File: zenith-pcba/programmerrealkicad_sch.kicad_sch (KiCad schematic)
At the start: 16 parts, among them SW1 G4R152312, U1 XC7A50T-CSG325, U3 CH347T, U4 TPS54302DDCT, U5 TPS54302DDCT, X1 SX5B8.000F1520F30

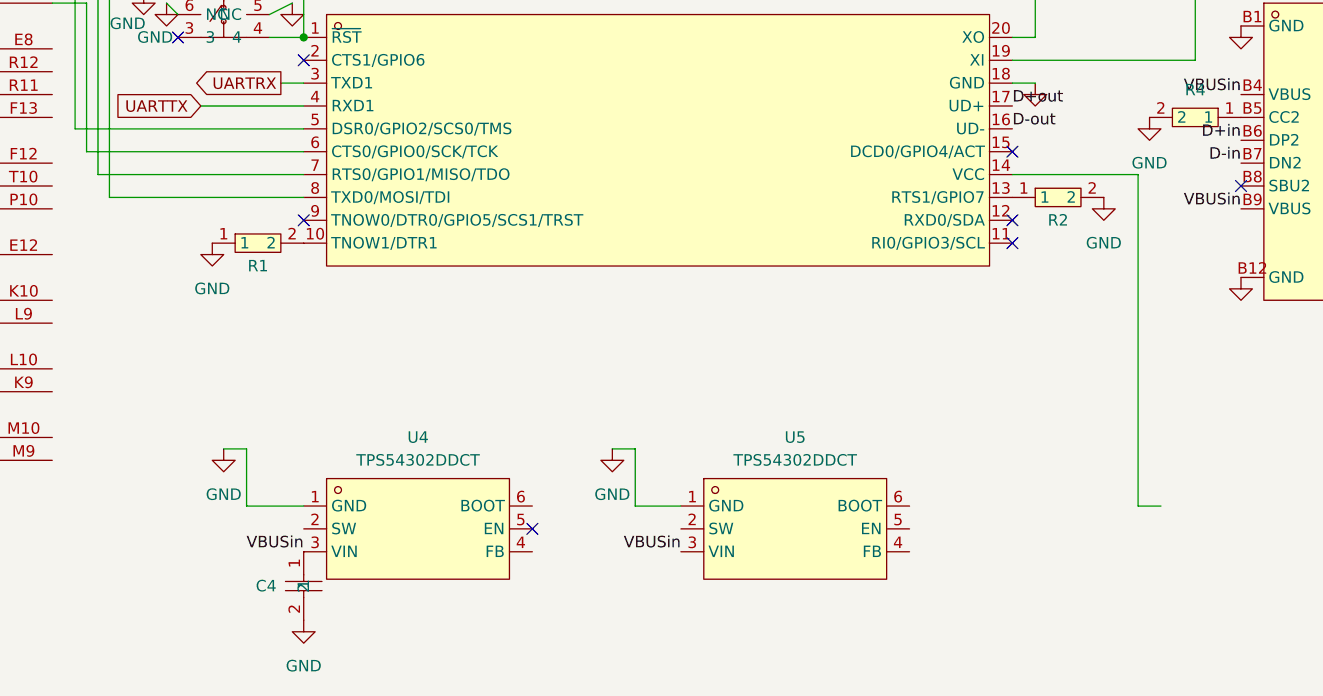
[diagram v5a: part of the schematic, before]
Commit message: feat(pcba): 3.3v buck
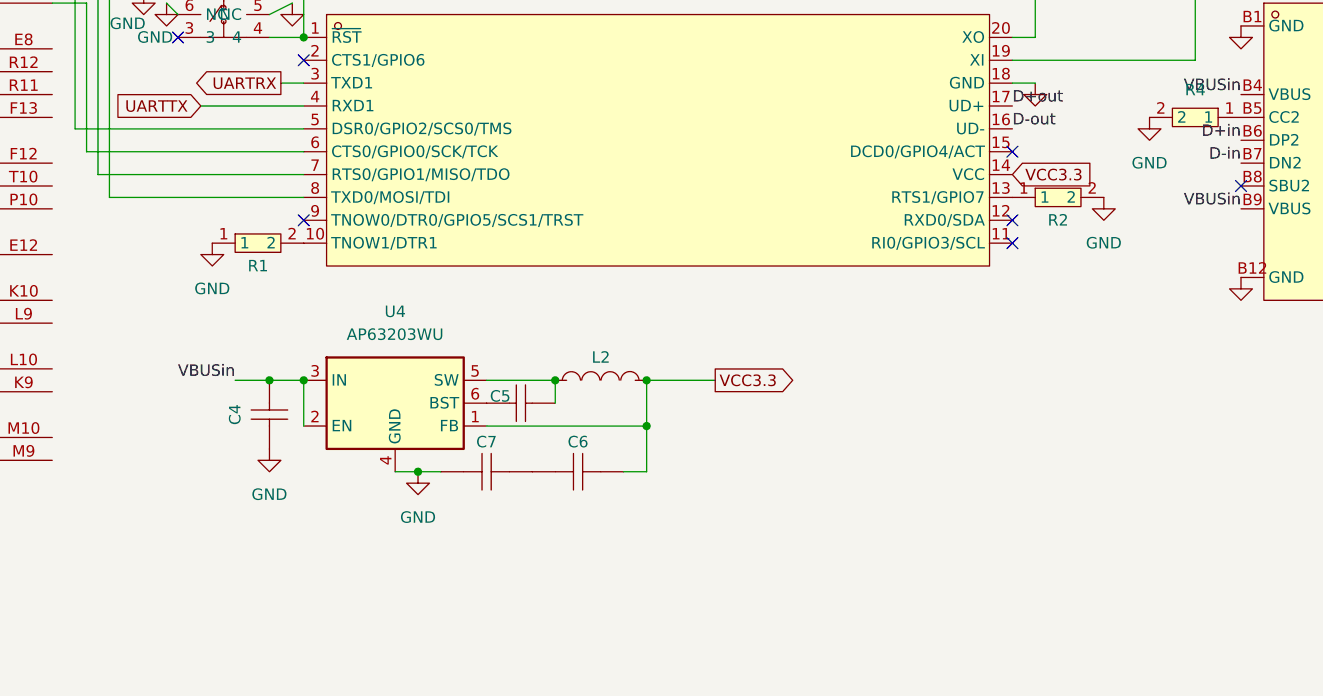
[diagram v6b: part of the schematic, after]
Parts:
- removed U4, U5: TPS54302DDCT, easyeda2kicad:TSOT-23-6_L2.9-W1.6-P0.95-LS2.8-BR, symbol easyeda2kicad:TPS54302DDCT
- added C5: CL10B104KA8NNNC, easyeda2kicad:C0603, symbol easyeda2kicad:CL10B104KA8NNNC
- added C6, C7: CC1206KKX7R6BB226, easyeda2kicad:C1206, symbol easyeda2kicad:CC1206KKX7R6BB226
- added L2: SWPA4030S3R3MT, easyeda2kicad:IND-SMD_L4.0-W4.0_SMNR4012, symbol easyeda2kicad:SWPA4030S3R3MT
- added U4: AP63203WU, Package_TO_SOT_SMD:TSOT-23-6, symbol Regulator_Switching:AP63203WU
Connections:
- net GND: now also C7.1, U4.4 (GND)
- net VBUSin: now also U4.2 (EN), U4.3 (IN)
- net VCC3.3: now reaches U3.14 (VCC)
- net VCC3.3: now also C6.2, L2.2, U4.1 (FB)
- new net: C5.2, L2.1, U4.5 (SW)
- new net: C5.1, U4.6 (BST)
- new net: C6.1, C7.2
- no-connect marks 10 -> 9

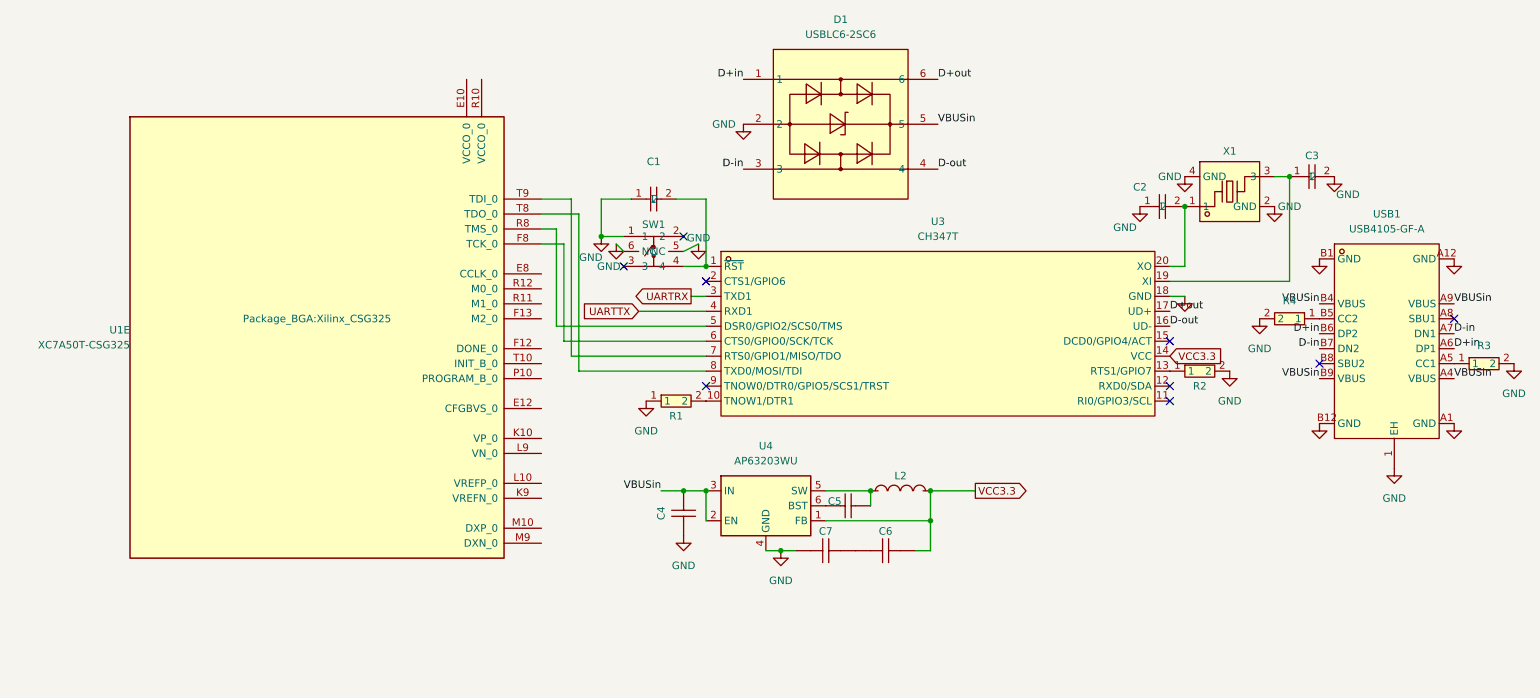
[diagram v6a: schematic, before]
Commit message: chore(pcba): import din connectors
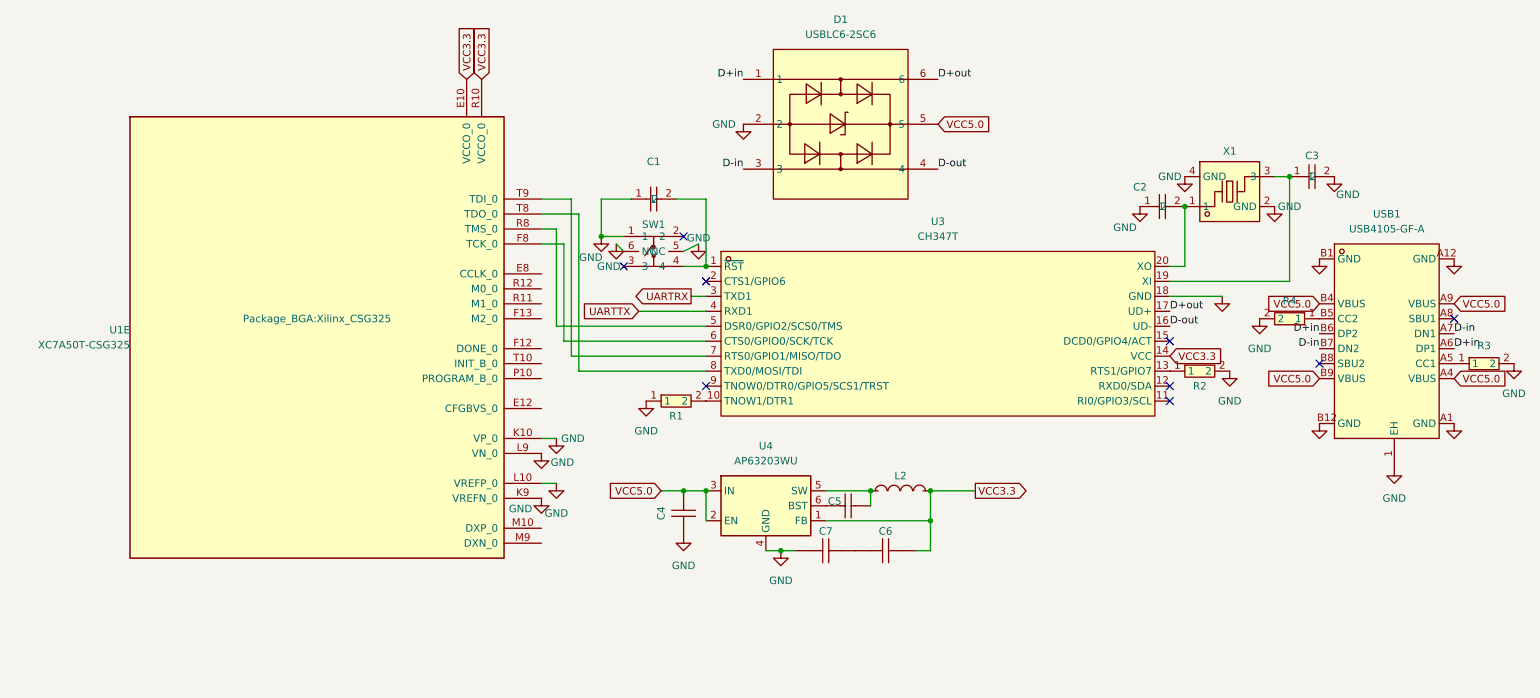
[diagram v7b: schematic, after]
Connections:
- net GND: now also U1.K10 (VP_0), U1.K9 (VREFN_0), U1.L10 (VREFP_0), U1.L9 (VN_0)
- net VCC3.3: now also U1.E10 (VCCO_0), U1.R10 (VCCO_0)
- net VBUSin renamed VCC5.0

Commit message: feat(pcba): migrate to kintex fpga
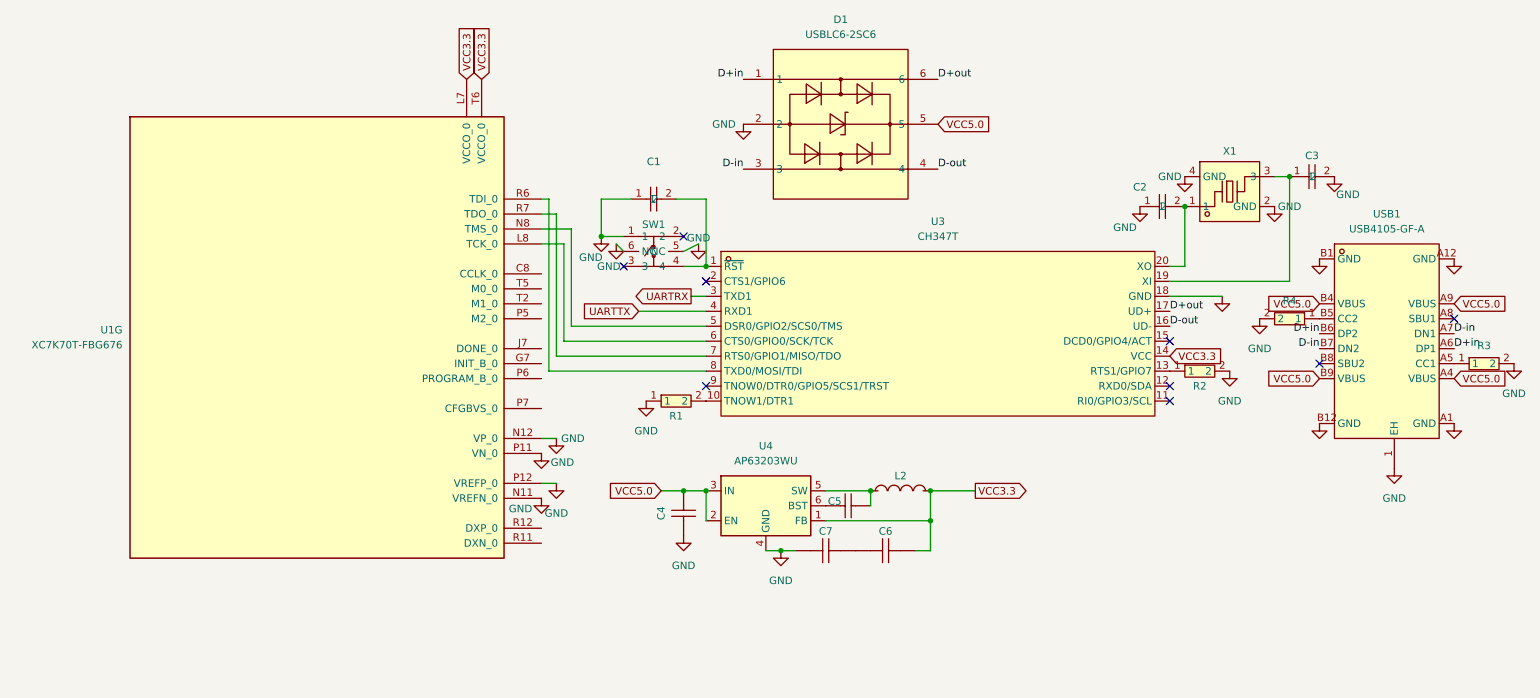
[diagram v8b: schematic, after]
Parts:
- removed U1: XC7A50T-CSG325, Package_BGA:Xilinx_CSG325, symbol FPGA_Xilinx_Artix7:XC7A50T-CSG325
- added U1: XC7K70T-FBG676, easyeda2kicad:FBGA-676_L27.0-W27.0-R26-C26-P1.00-BL, symbol FPGA_Xilinx_Kintex7:XC7K70T-FBG676
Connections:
- net GND: now also U1.N11 (VREFN_0), U1.N12 (VP_0), U1.P11 (VN_0), U1.P12 (VREFP_0)
- net VCC3.3: now also U1.L7 (VCCO_0), U1.T6 (VCCO_0)
- net at U3.5 (DSR0/GPIO2/SCS0/TMS): now also U1.N8 (TMS_0)
- net at U3.6 (CTS0/GPIO0/SCK/TCK): now also U1.L8 (TCK_0)
- net at U3.7 (RTS0/GPIO1/MISO/TDO): now also U1.R7 (TDO_0)
- net at U3.8 (TXD0/MOSI/TDI): now also U1.R6 (TDI_0)
